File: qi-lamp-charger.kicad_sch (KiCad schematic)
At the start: 82 parts, among them J1 Conn_01x03, J2 Conn_01x02, J4 Conn_01x06, J5 Conn_01x03, Q1 BSS308PE H6327, SW1 SKTDLDE010, U1 SLG5NV1430V, U2 BQ51050BRHL, U3 ESP-12E

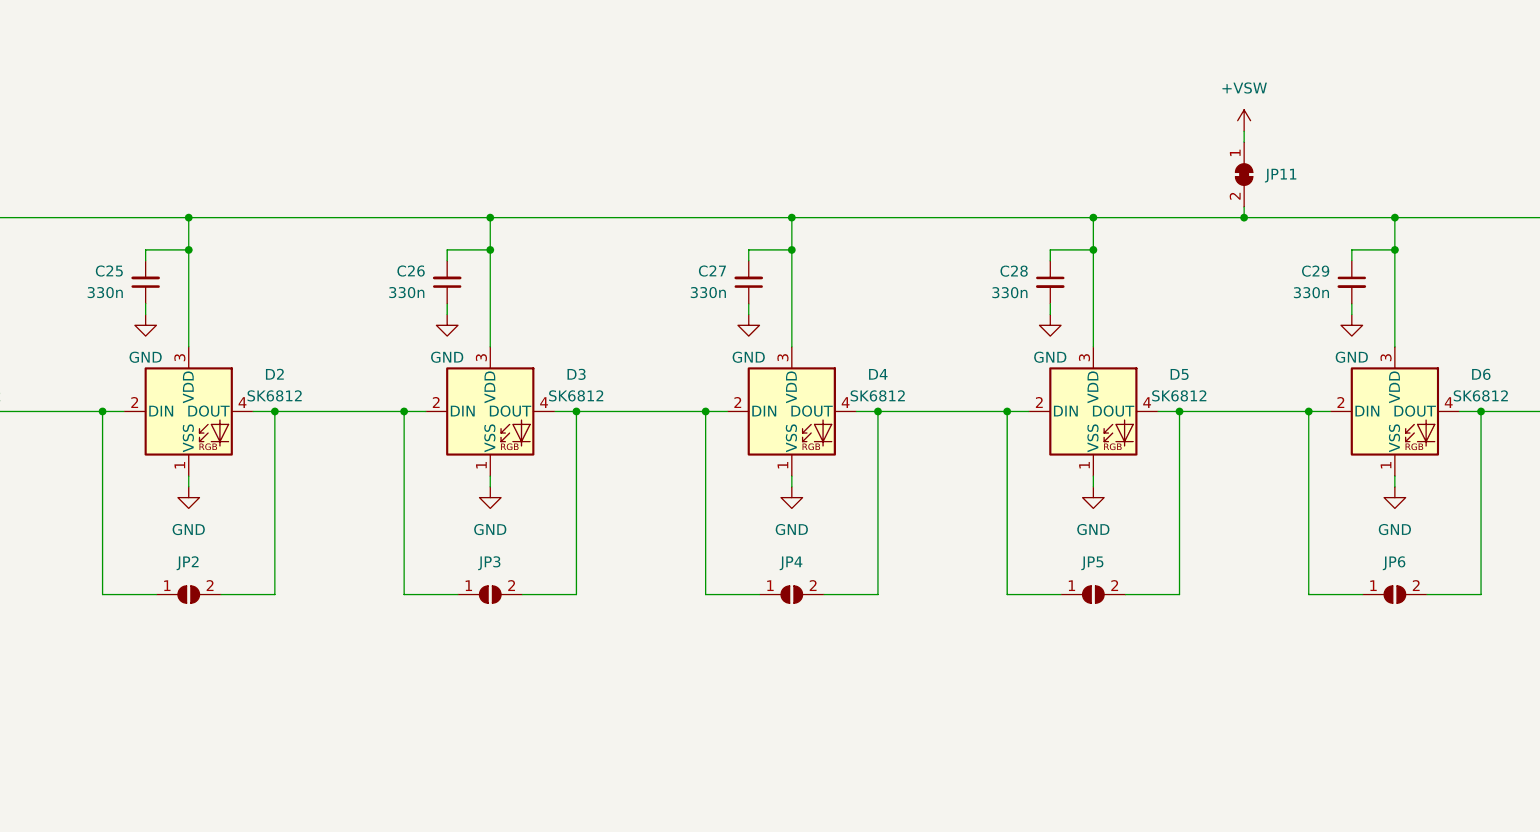
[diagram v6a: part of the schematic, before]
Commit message: Puzzle #4 - has GPIO0 brainfart
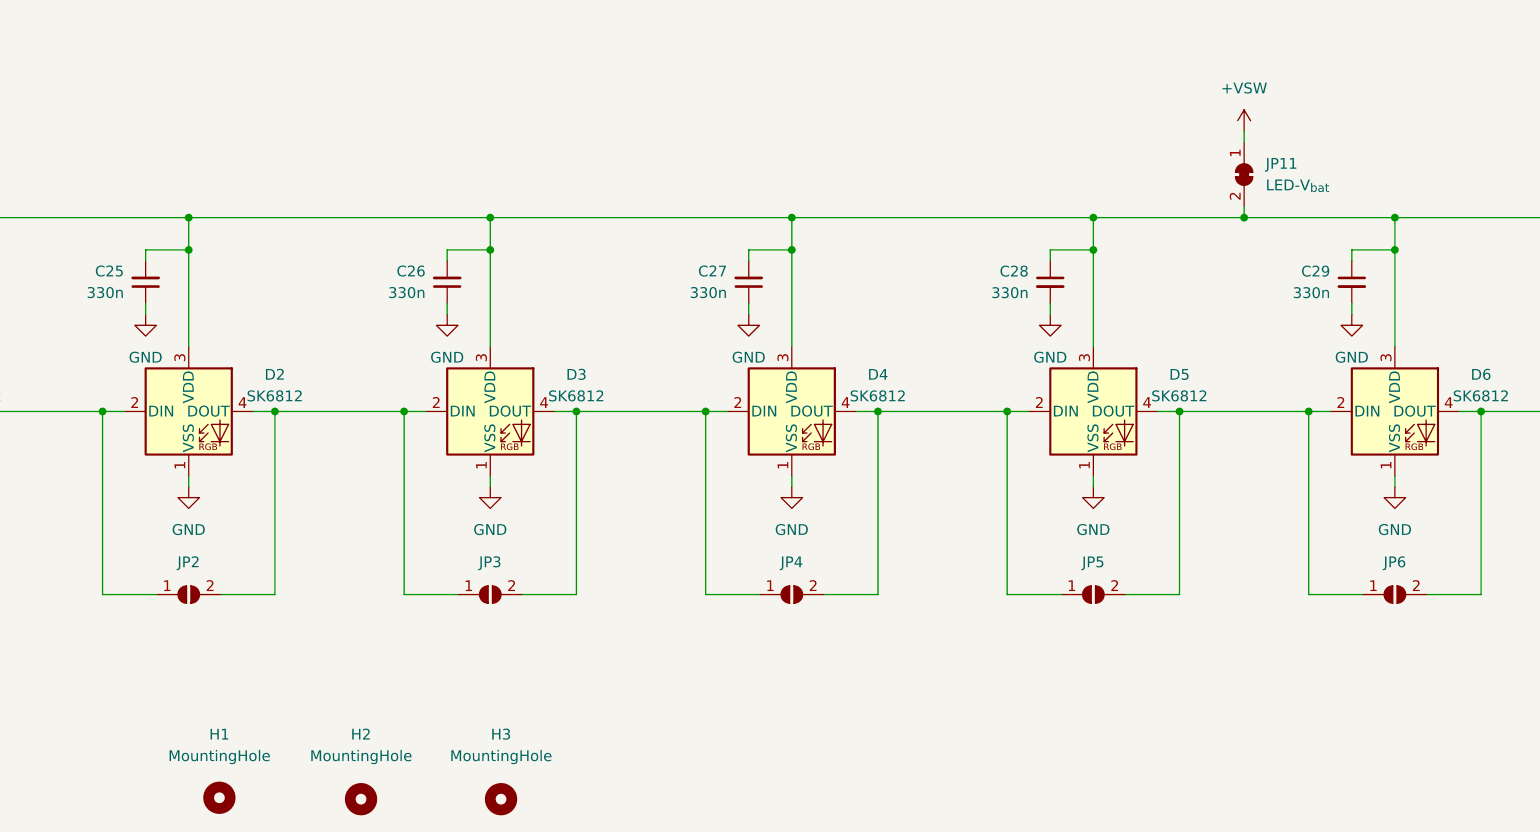
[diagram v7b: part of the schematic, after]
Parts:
- added H1, H2, H3: MountingHole, MountingHole:MountingHole_3.2mm_M3_ISO14580, symbol Mechanical:MountingHole
- JP11: silk_text (none) -> LED-V_{bat}
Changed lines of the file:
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@@
+    )
+  )
+  (symbol (lib_id "Mechanical:MountingHole") (at 119.38 269.24 0) (unit 1)
+    (in_bom yes) (on_board yes) (fields_autoplaced)
+    (property "Reference" "H3" (id 0) (at 119.38 261.62 0))
+    (property "Value" "MountingHole" (id 1) (at 119.38 264.16 0))
+    (property "Footprint" "MountingHole:MountingHole_3.2mm_M3_ISO14580" (id 2) (at 119.38 269.24 0)
+      (effects (font (size 1.27 1.27)) hide)
+    )
+    (property "Datasheet" "~" (id 3) (at 119.38 269.24 0)
+      (effects (font (size 1.27 1.27)) hide)
     )
   )
@@
     (pin "2")
   )
+  (symbol (lib_id "Mechanical:MountingHole") (at 102.87 269.24 0) (unit 1)
+    (in_bom yes) (on_board yes) (fields_autoplaced)
+    (property "Reference" "H2" (id 0) (at 102.87 261.62 0))
+    (property "Value" "MountingHole" (id 1) (at 102.87 264.16 0))
+    (property "Footprint" "MountingHole:MountingHole_3.2mm_M3_ISO14580" (id 2) (at 102.87 269.24 0)
+      (effects (font (size 1.27 1.27)) hide)
+    )
+    (property "Datasheet" "~" (id 3) (at 102.87 269.24 0)
+      (effects (font (size 1.27 1.27)) hide)
+    )
+  )
   (symbol (lib_id "power:GND") (at 189.23 232.41 0) (unit 1)
     (in_bom yes) (on_board yes) (fields_autoplaced)
@@
   (symbol (lib_id "Jumper:SolderJumper_2_Bridged") (at 207.01 195.58 90) (mirror x) (unit 1)
     (in_bom yes) (on_board yes) (fields_autoplaced)
-    (property "Reference" "JP11" (id 0) (at 209.55 195.5799 90)
+    (property "Reference" "JP11" (id 0) (at 209.55 194.3099 90)
       (effects (font (size 1.27 1.27)) (justify right))
     )
@@
     (property "fit_field" "DNP" (id 4) (at 207.01 195.58 0)
       (effects (font (size 1.27 1.27)) hide)
+    )
+    (property "silk_text" "LED-V_{bat}" (id 5) (at 209.55 196.8499 90)
+      (effects (font (size 1.27 1.27)) (justify right))
     )
     (pin "1")
@@
     (pin "1")
   )
+  (symbol (lib_id "Mechanical:MountingHole") (at 86.1673 269.0743 0) (unit 1)
+    (in_bom yes) (on_board yes) (fields_autoplaced)
+    (property "Reference" "H1" (id 0) (at 86.1673 261.62 0))
+    (property "Value" "MountingHole" (id 1) (at 86.1673 264.16 0))
+    (property "Footprint" "MountingHole:MountingHole_3.2mm_M3_ISO14580" (id 2) (at 86.1673 269.0743 0)
+      (effects (font (size 1.27 1.27)) hide)
+    )
+    (property "Datasheet" "~" (id 3) (at 86.1673 269.0743 0)
+      (effects (font (size 1.27 1.27)) hide)
+    )
+  )
   (symbol (lib_id "Device:C_Small") (at 72.39 60.96 0) (unit 1)
     (in_bom yes) (on_board yes) (fields_autoplaced)
@@
       (reference "D12") (unit 1) (value "CD0603-B0340R") (footprint "Diode_SMD:D_0603_1608Metric")
     )
+    (path "/e5110ee0-872f-4d65-9b53-e4975e9dbe4c"
+      (reference "H1") (unit 1) (value "MountingHole") (footprint "MountingHole:MountingHole_3.2mm_M3_ISO14580")
+    )
+    (path "/823328e5-53cf-4d29-8cb5-21a9f83062fb"
+      (reference "H2") (unit 1) (value "MountingHole") (footprint "MountingHole:MountingHole_3.2mm_M3_ISO14580")
+    )
+    (path "/01b8118f-962f-4335-8b79-6e89c5fec856"
+      (reference "H3") (unit 1) (value "MountingHole") (footprint "MountingHole:MountingHole_3.2mm_M3_ISO14580")
+    )
     (path "/5692bf59-80e3-4420-a260-8a77be664c2a"

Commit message: Puzzle #5
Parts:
- removed D12: CD0603-B0340R, Diode_SMD:D_0603_1608Metric, symbol Device:D_Small_Filled
- R10, R11, R12, R13, R9: value 10k -> 20k
- R14: value 1M -> 20k
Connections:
- net DTR: no longer Q1.1 (G), R14.1, SW1.2
- net GND: now also J5.1 (Pin_1); no longer J5.3 (Pin_3)
- net LED_V+: now also J5.3 (Pin_3); no longer J5.1 (Pin_1)
- net BTN: now reaches U3.5 (GPIO14)
- net BTN: now also Q1.1 (G), R14.1, SW1.2
- no-connect marks 11 -> 10
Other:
- moved on the sheet: C22, C23, C34, J1, J4, J5, JP12, R10, R11, R13, R14, R9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
